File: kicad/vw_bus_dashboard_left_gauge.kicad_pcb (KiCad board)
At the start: 2 copper layers, 86 x 57.5 mm, 26 parts, among them J1 Conn_01x04, J2 Conn_01x01, J3 Conn_01x01, J4 Conn_01x01, J5 Conn_01x01, U1 TLC59116-Q1

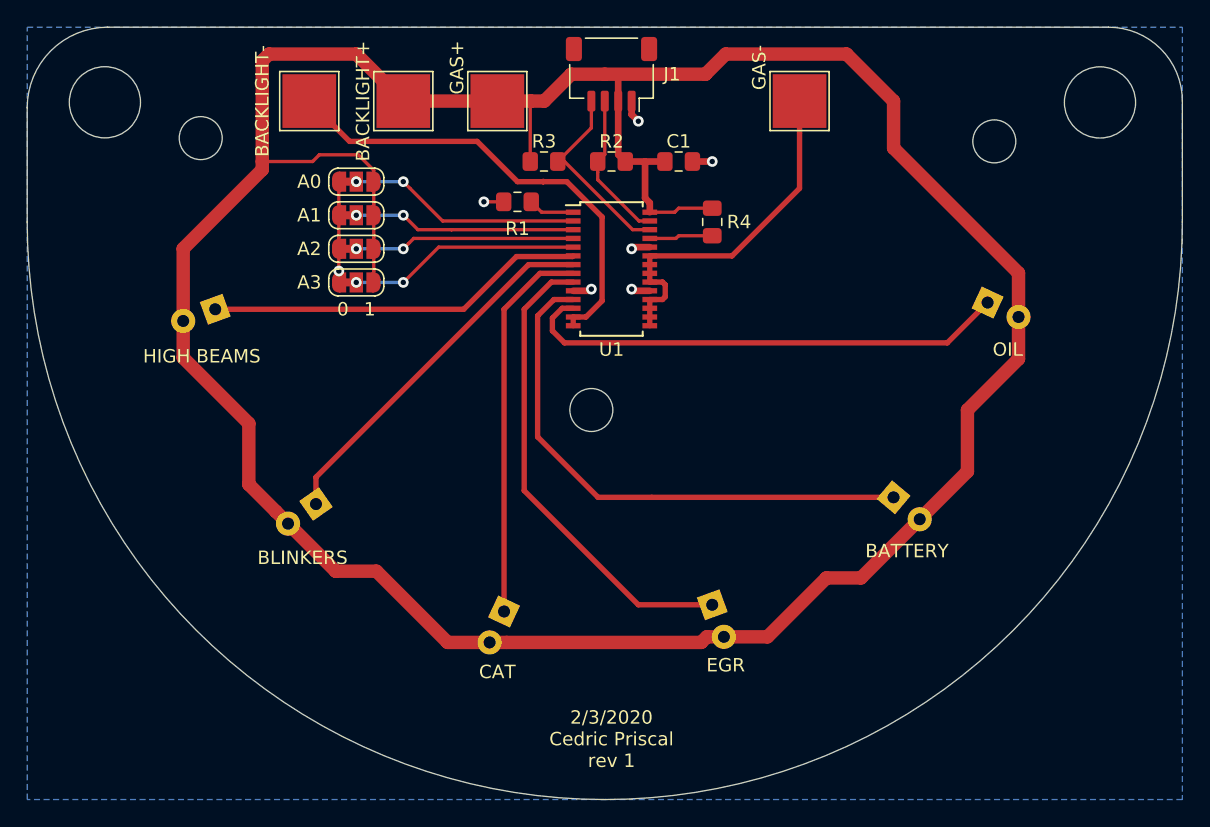
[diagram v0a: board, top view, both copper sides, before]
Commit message: Rev 2 using NeoPixels
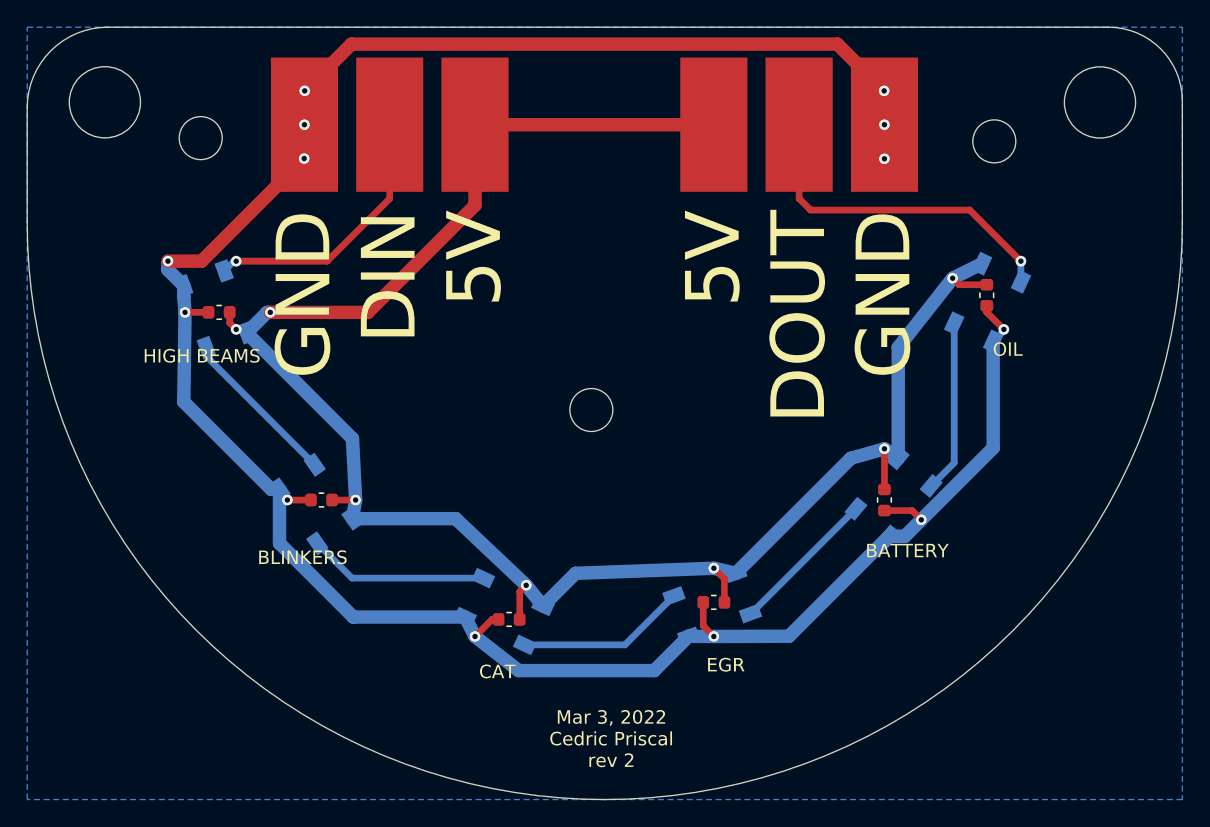
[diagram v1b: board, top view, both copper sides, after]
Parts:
- removed the J1 at (155.9, 73.1)
- removed JP1, JP2, JP3, JP4: SolderJumper_3_Bridged12, Jumper:SolderJumper-3_P1.3mm_Bridged12_RoundedPad1.0x1.5mm_NumberLabels
- removed R1, R2, R3, R4: R_US, Resistor_SMD:R_0805_2012Metric_Pad1.15x1.40mm_HandSolder
- removed U1: TLC59116-Q1, Package_SO:TSSOP-28_4.4x9.7mm_P0.65mm
- added C2: C, Capacitor_SMD:C_0603_1608Metric, F.Cu at (134.3, 104.8)
- added C3: C, Capacitor_SMD:C_0603_1608Metric, F.Cu at (148.3, 113.7)
- added C4: C, Capacitor_SMD:C_0603_1608Metric, F.Cu at (163.5, 112.4)
- added C5: C, Capacitor_SMD:C_0603_1608Metric, F.Cu at (176.2, 104.8)
- added C6: C, Capacitor_SMD:C_0603_1608Metric, F.Cu at (183.8, 89.6)
- added J4: Conn_01x01, Connector_Wire:SolderWirePad_1x01_SMD_5x10mm, F.Cu at (169.9, 76.9)
- added J6: Conn_01x01, Connector_Wire:SolderWirePad_1x01_SMD_5x10mm, F.Cu at (176.2, 76.9)
- C1: value 0.1u -> C; footprint Capacitor_SMD:C_0805_2012Metric_Pad1.15x1.40mm_HandSolder -> Capacitor_SMD:C_0603_1608Metric
- D1, D2, D3, D4: value LED RED -> WS2812B; footprint LED_THT:LED_D5.0mm -> LED_SMD:LED_WS2812B_PLCC4_5.0x5.0mm_P3.2mm
- D5: value LED GREEN -> WS2812B; footprint LED_THT:LED_D5.0mm -> LED_SMD:LED_WS2812B_PLCC4_5.0x5.0mm_P3.2mm
- D6: value LED BLUE -> WS2812B; footprint LED_THT:LED_D5.0mm -> LED_SMD:LED_WS2812B_PLCC4_5.0x5.0mm_P3.2mm
- J1: renamed from J4; footprint TestPoint:TestPoint_Pad_4.0x4.0mm -> Connector_Wire:SolderWirePad_1x01_SMD_5x10mm
- J2, J3, J5: footprint TestPoint:TestPoint_Pad_4.0x4.0mm -> Connector_Wire:SolderWirePad_1x01_SMD_5x10mm
- moved C1 36.0 mm to (126.7, 90.8), turned to 180 degrees
- moved J3 30.6 mm to (139.4, 76.9)
- moved J2 16.2 mm to (163.5, 76.9)
- moved J1 5.62 mm to (145.7, 76.9)
- moved J5 1.80 mm to (133.0, 76.9)
- turned D1 to 110 degrees
- turned D2 to 125 degrees
- turned D3 to 155 degrees
- turned D4 to 200 degrees
- turned D5 to 230 degrees
- turned D6 to 245 degrees
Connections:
- C1 pad 1: +3V3 -> +5V
- D1 pad 1: Net-(D1-Pad1) -> +5V
- D1 pad 2: +3V3 -> Net-(D1-Pad2)
- D2 pad 1: Net-(D2-Pad1) -> +5V
- D2 pad 2: +3V3 -> Net-(D2-Pad2)
- D3 pad 1: Net-(D3-Pad1) -> +5V
- D3 pad 2: +3V3 -> Net-(D3-Pad2)
- D4 pad 1: Net-(D4-Pad1) -> +5V
- D4 pad 2: +3V3 -> Net-(D4-Pad2)
- D5 pad 1: Net-(D5-Pad1) -> +5V
- D5 pad 2: +3V3 -> Net-(D5-Pad2)
- D6 pad 1: Net-(D6-Pad1) -> +5V
- D6 pad 2: +3V3 -> Net-(D6-Pad2)
- J1 pad 1: +3V3 -> +5V
- J2 pad 1: +3V3 -> +5V
- J3 pad 1: Net-(J3-Pad1) -> Net-(D1-Pad4)
- J5 pad 1: Net-(J5-Pad1) -> GND
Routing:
- net +3V3: track 225.4 -> 0.00 mm
- net GND: track 16.4 -> 179.9 mm, vias 7 -> 13
- net +5V: track 0.00 -> 142.8 mm, vias 0 -> 7
- net Net-(D5-Pad1): track 40.5 -> 0.00 mm
- net Net-(D6-Pad1): track 36.8 -> 0.00 mm
- net Net-(D4-Pad1): track 35.5 -> 0.00 mm
- net Net-(J5-Pad1): track 34.9 -> 0.00 mm
- net Net-(D3-Pad1): track 28.8 -> 0.00 mm
- net Net-(D1-Pad1): track 28.3 -> 0.00 mm
- net Net-(D2-Pad1): track 27.7 -> 0.00 mm
- net Net-(J3-Pad1): track 27.0 -> 0.00 mm
- net Net-(D6-Pad2): track 0.00 -> 25.5 mm, vias 0 -> 1
- net Net-(D1-Pad4): track 0.00 -> 20.1 mm, vias 0 -> 1
- net Net-(JP1-Pad2): track 17.4 -> 0.00 mm, vias 2 -> 0
- net Net-(JP4-Pad2): track 17.2 -> 0.00 mm, vias 2 -> 0
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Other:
- board text added: "5V"
- board text added: "DIN"
- board text added: "DOUT"
- board text added: "GND"
- board text added: "Mar 3, 2022 Cedric Priscal rev 2"
- board text removed: "0"
- board text removed: "1"
- board text removed: "2/3/2020 Cedric Priscal rev 1"
- board text removed: "A0"
- board text removed: "A1"
- board text removed: "A2"
- board text removed: "A3"
- board text removed: "BACKLIGHT+"
- board text removed: "BACKLIGHT-"
- board text removed: "GAS+"
- board text removed: "GAS-"
